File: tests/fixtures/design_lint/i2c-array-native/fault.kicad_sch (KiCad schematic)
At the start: 2 parts, among them U1 I2C target

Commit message: Bind mapped I2C arrays to part identity
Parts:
- RN1: PART_ID (none) -> SYNTHETIC-ARRAY-47K
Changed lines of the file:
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@@
     (property "Value" "4x4.7k" (at 100 91.44 0) (effects (font (size 1.27 1.27)) (justify left)))
     (property "Footprint" "Synthetic:RA4" (at 100 100 0) (effects (font (size 1.27 1.27)) hide))
+    (property "PART_ID" "SYNTHETIC-ARRAY-47K" (at 100 100 0) (effects (font (size 1.27 1.27)) hide))
     (property "Datasheet" "" (at 100 100 0) (effects (font (size 1.27 1.27)) hide))
     (pin "1")

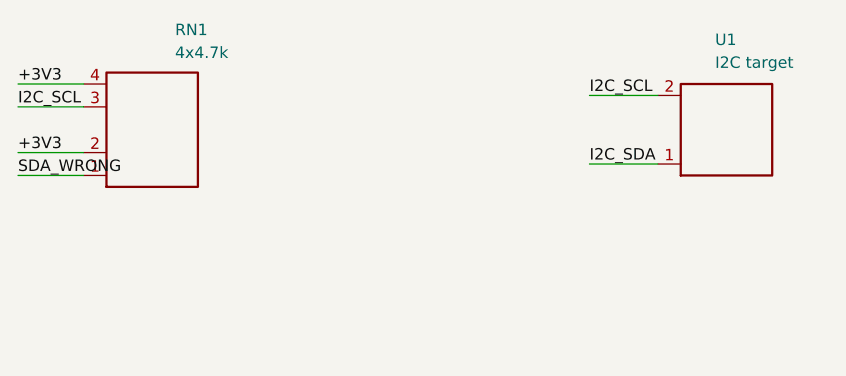
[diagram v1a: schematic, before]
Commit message: Allow explicitly mapped non-C I2C capacitance refs
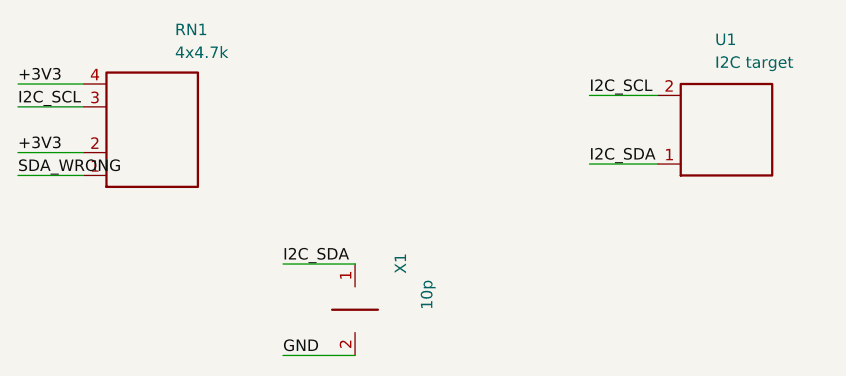
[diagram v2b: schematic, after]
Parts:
- added X1: 10p, Synthetic:0603, symbol Device:C
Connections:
- net I2C_SDA: now also X1.1
- new net GND: X1.2
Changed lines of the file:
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@@
     (instances (project "synthetic-i2c-pullup-array"
       (path "/72000000-0000-4000-8000-000000000001" (reference "U1") (unit 1)))))
+  (symbol (lib_id "Device:C") (at 120 120 0) (unit 1)
+    (in_bom yes) (on_board yes) (dnp no)
+    (property "Reference" "X1" (at 125.08 116 90) (effects (font (size 1.27 1.27)) (justify left)))
+    (property "Value" "10p" (at 128 120 90) (effects (font (size 1.27 1.27)) (justify left)))
+    (property "Footprint" "Synthetic:0603" (at 120 120 0) (effects (font (size 1.27 1.27)) hide))
+    (property "Datasheet" "" (at 120 120 0) (effects (font (size 1.27 1.27)) hide))
+    (pin "1")
+    (pin "2")
+    (instances (project "synthetic-i2c-pullup-array"
+      (path "/72000000-0000-4000-8000-000000000001" (reference "X1") (unit 1)))))
+  (wire (pts (xy 120 114.92) (xy 112 114.92))
+    (stroke (width 0) (type default)))
+  (label "I2C_SDA" (at 112 114.92 0)
+    (effects (font (size 1.27 1.27)) (justify left bottom))
+)
+  (wire (pts (xy 120 125.08) (xy 112 125.08))
+    (stroke (width 0) (type default)))
+  (label "GND" (at 112 125.08 0)
+    (effects (font (size 1.27 1.27)) (justify left bottom))
+)
   (wire (pts (xy 89.84 105.08) (xy 82.55 105.08))
     (stroke (width 0) (type default)))

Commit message: Discover mapped I2C capacitors by symbol identity
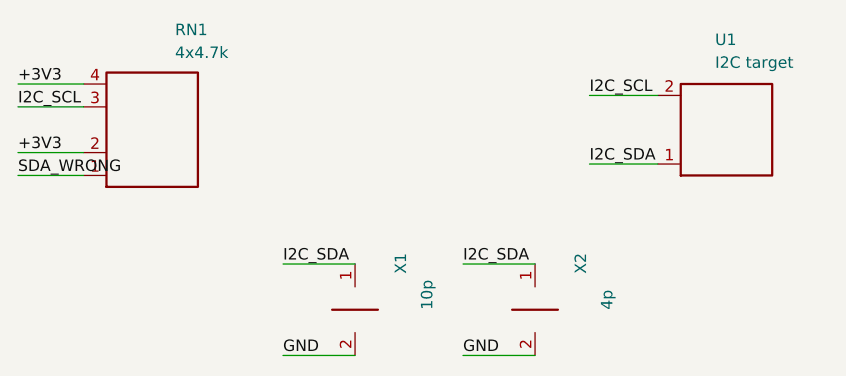
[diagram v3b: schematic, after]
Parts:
- added X2: 4p, Synthetic:0603, symbol Device:C
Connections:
- net GND: now also X2.2
- net I2C_SDA: now also X2.1
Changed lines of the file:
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@@
+    (effects (font (size 1.27 1.27)) (justify left bottom))
+)
+  (symbol (lib_id "Device:C") (at 140 120 0) (unit 1)
+    (in_bom yes) (on_board yes) (dnp no)
+    (property "Reference" "X2" (at 145.08 116 90) (effects (font (size 1.27 1.27)) (justify left)))
+    (property "Value" "4p" (at 148 120 90) (effects (font (size 1.27 1.27)) (justify left)))
+    (property "Footprint" "Synthetic:0603" (at 140 120 0) (effects (font (size 1.27 1.27)) hide))
+    (property "Datasheet" "" (at 140 120 0) (effects (font (size 1.27 1.27)) hide))
+    (pin "1")
+    (pin "2")
+    (instances (project "synthetic-i2c-pullup-array"
+      (path "/72000000-0000-4000-8000-000000000001" (reference "X2") (unit 1)))))
+  (wire (pts (xy 140 114.92) (xy 132 114.92))
+    (stroke (width 0) (type default)))
+  (label "I2C_SDA" (at 132 114.92 0)
+    (effects (font (size 1.27 1.27)) (justify left bottom))
+)
+  (wire (pts (xy 140 125.08) (xy 132 125.08))
+    (stroke (width 0) (type default)))
+  (label "GND" (at 132 125.08 0)
     (effects (font (size 1.27 1.27)) (justify left bottom))
 )
